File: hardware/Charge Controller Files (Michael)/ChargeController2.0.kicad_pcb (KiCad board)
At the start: 2 copper layers, 90 parts, among them J1 GND_TEST_01x01_Pin, J10 SOL_TEST_01x01_Pin, J13 Conn-1x2, J14 Conn-1x2, J15 Conn-1x2, J17 SCL_MAS_01x01_Pin, J18 SDA_MAS_01x01_Pin, J19 SYS-1x2, J2 SP_01x02_Pin, J3 BATT_TEST_01x01_Pin, J4 3.3V_PULLUP_01x02_Pin, J5 BATT_01x02_Pin, J6 Conn-1x2, J7 Conn-1x2, J8 Conn-1x2, J9 SYS_TEST_01x01_Pin, Q1 SI2318DS-T1-E3, Q10 SI2318DS-T1-E3, Q11 SI2318DS-T1-E3, Q12 SI2318DS-T1-E3, Q2 SI2318DS-T1-E3, Q3 SI2318DS-T1-E3, Q4 SI2318DS-T1-E3, Q5 AONS66614, Q6 AONS66614, Q7 AONS66614, Q8 AONS66614, Q9 SI2318DS-T1-E3, SW1 100SP1T1B1M1QEH, U1 BQ25756ERRVR

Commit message: First Update
Prelim layout
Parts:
- moved C22 123.2 mm to (40.3, 41.0)
- moved J4 114.3 mm to (18.5, 25.5)
- moved J14 113.9 mm to (42.0, 25.0)
- moved J2 113.9 mm to (17.5, 15.5)
- moved J8 113.3 mm to (33.5, 25.0)
- moved J6 112.6 mm to (28.0, 15.5)
- moved J15 111.2 mm to (52.5, 15.5)
- moved J13 110.5 mm to (44.0, 15.5)
- moved J7 109.4 mm to (36.0, 15.5)
- moved R22 109.1 mm to (62.5, 35.1)
- moved R25 109.1 mm to (62.5, 37.6)
- moved R26 109.1 mm to (62.5, 40.1)
- moved R_AC2 109.1 mm to (62.5, 45.2)
- moved R_AC3 109.1 mm to (67.0, 56.4)
- moved R_FBG1 109.1 mm to (62.5, 47.7)
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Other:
- board outline added: 90.2 x 95.9 mm

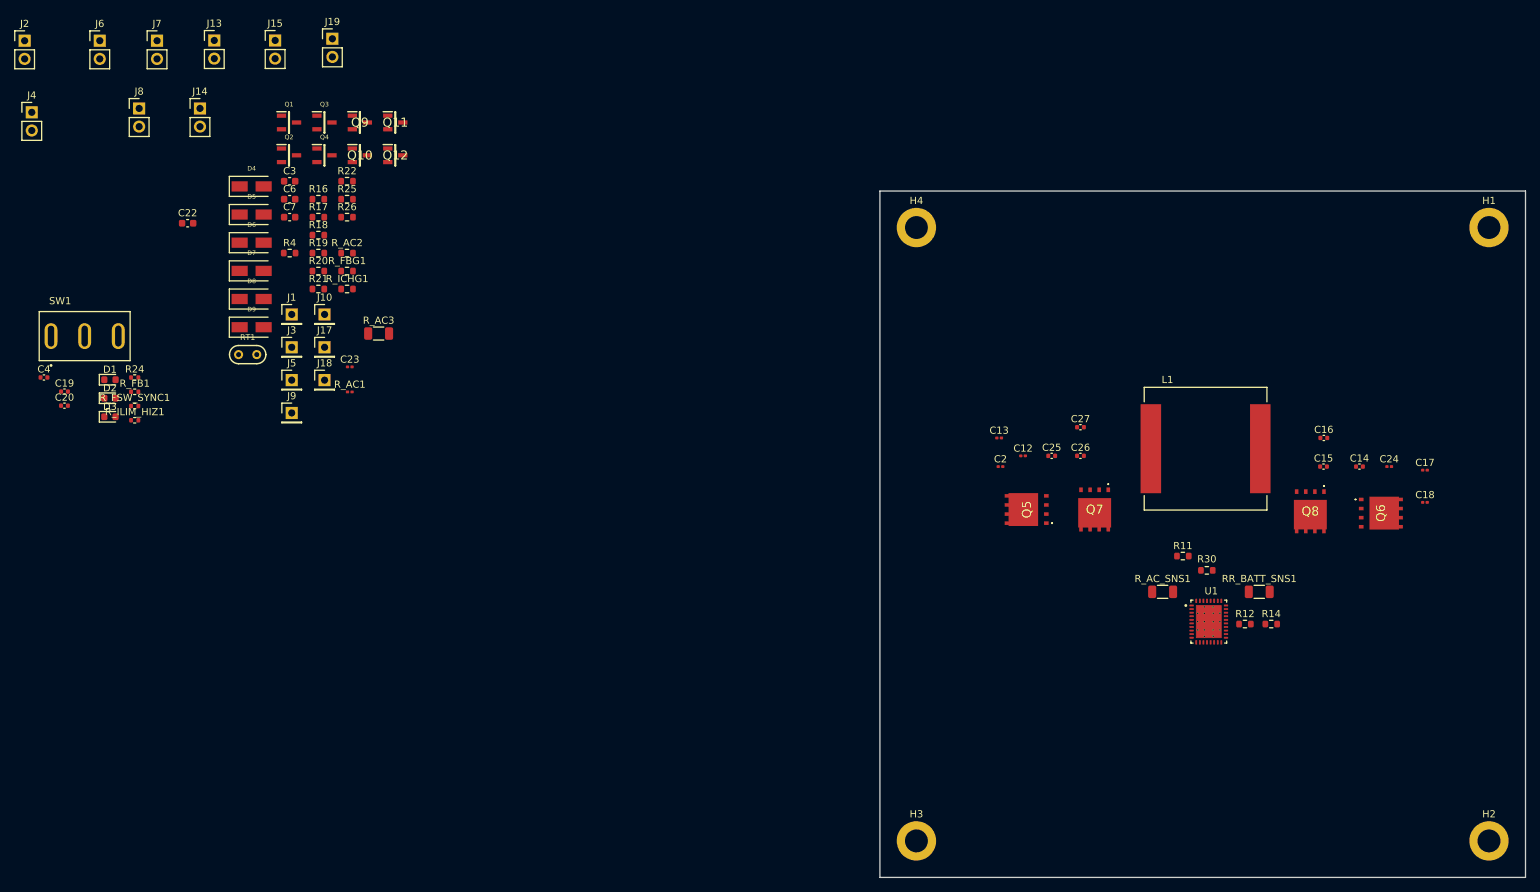
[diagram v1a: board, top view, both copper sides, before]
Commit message: Diode/Small Fixes
- Changed Inhibits MOSFETs to all be same footprint
- Changing diodes
   - Inhibits/Power Path -> SS24
   - Bootstrap -> BAT54
- LODRV_1 pin incorrectly placed
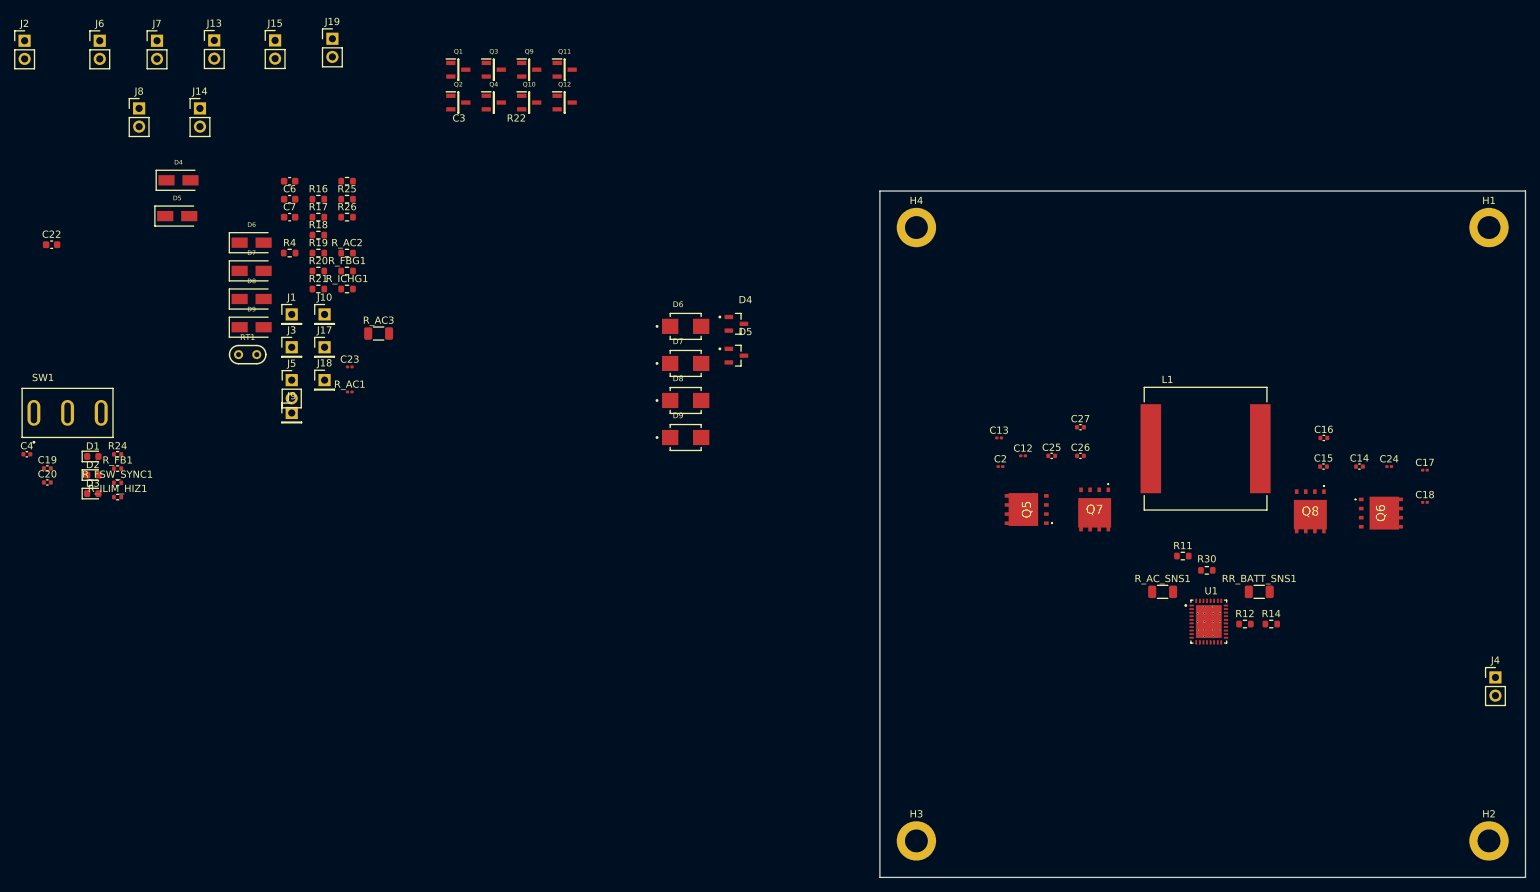
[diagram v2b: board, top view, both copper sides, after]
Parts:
- added D4: BAT54, bmsfootprints:BAT54, F.Cu at (116.9, 55.0)
- added D5: BAT54, bmsfootprints:BAT54, F.Cu at (116.9, 59.5)
- added D6: SS24, bmsfootprints:SS24, F.Cu at (109.9, 55.4)
- added D7: SS24, bmsfootprints:SS24, F.Cu at (109.9, 60.6)
- added D8: SS24, bmsfootprints:SS24, F.Cu at (109.9, 65.8)
- added D9: SS24, bmsfootprints:SS24, F.Cu at (109.9, 70.9)
- J5: footprint Connector_PinHeader_2.54mm:PinHeader_1x01_P2.54mm_Vertical -> Connector_PinHeader_2.54mm:PinHeader_1x02_P2.54mm_Vertical
- Q10, Q11, Q12, Q9: footprint bmsfootprints:SOT95P237X102-3N -> bmsfootprints:SI2318DS-T1-E3
- moved J4 219.2 mm to (223.0, 104.5)
- moved Q1 24.8 mm to (78.1, 19.6)
- moved Q10 24.8 mm to (88.0, 24.1)
- moved Q11 24.8 mm to (93.0, 19.6)
- moved Q12 24.8 mm to (93.0, 24.1)
- moved Q2 24.8 mm to (78.1, 24.1)
- moved Q3 24.8 mm to (83.0, 19.6)
- moved Q4 24.8 mm to (83.0, 24.1)
- moved Q9 24.8 mm to (88.0, 19.6)
- moved C22 19.2 mm to (21.3, 44.0)
- moved C19 11.0 mm to (20.7, 75.2)
- moved C20 11.0 mm to (20.7, 77.2)
- moved C4 11.0 mm to (17.8, 73.3)
- moved D1 11.0 mm to (27.0, 73.6)
- moved D2 11.0 mm to (27.0, 76.2)
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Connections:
- Q7 pad 1: /LODRV_1 -> GND
- Q7 pad 4: GND -> /LODRV_1

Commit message: PCB First Draft
First Draft of PCB
Notes:
- Inhibits layout could use work
- No gorund plane, unfinished
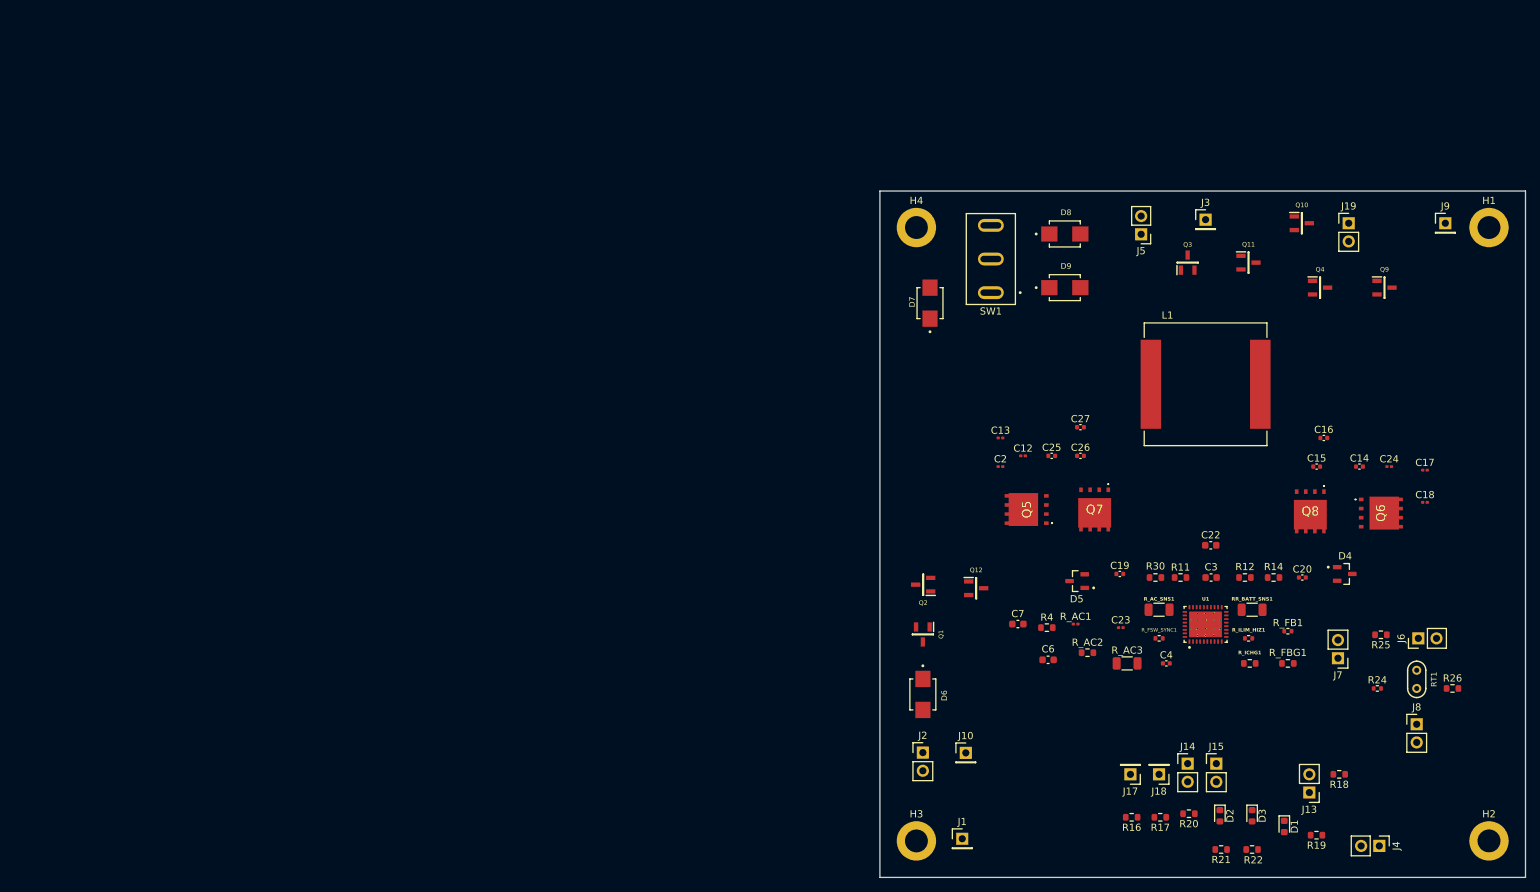
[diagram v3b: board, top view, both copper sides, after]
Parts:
- removed the D4 at (39.0, 35.0)
- removed the D5 at (38.8, 40.0)
- removed the D6 at (49.2, 43.7)
- removed the D7 at (49.2, 47.7)
- removed the D8 at (49.2, 51.6)
- removed the D9 at (49.2, 55.5)
- R_AC3: value 53.25 -> 53.25k
- moved J6 202.3 mm to (212.2, 99.0), turned to 90 degrees
- moved J8 198.2 mm to (212.0, 111.0)
- moved J7 186.2 mm to (201.0, 101.8), turned to 180 degrees
- moved J13 185.6 mm to (197.0, 120.5), turned to 180 degrees
- moved R24 179.0 mm to (206.5, 106.0)
- moved C20 175.8 mm to (196.0, 90.5)
- moved D1 174.3 mm to (193.5, 125.3), turned to -90 degrees
- moved RT1 169.5 mm to (212.0, 104.7), turned to -90 degrees
- moved D3 168.1 mm to (189.0, 123.8), turned to -90 degrees
- moved R26 167.9 mm to (217.0, 106.0)
- moved C22 167.3 mm to (183.2, 86.0)
- moved J15 165.8 mm to (184.0, 116.5)
- moved J14 165.6 mm to (180.0, 116.5)
- moved R_FB1 165.1 mm to (194.0, 98.0)
- moved D2 164.5 mm to (184.5, 123.8), turned to -90 degrees
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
